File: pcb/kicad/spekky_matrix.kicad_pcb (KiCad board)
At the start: 2 copper layers, 153 x 95.8 mm, 330 parts, among them J1 USB_B_Micro, J2 Conn_ARM_JTAG_SWD_10, Q1 DMP3125L-7, Q2 DMP3125L-7, Q3 DMP3125L-7, Q4 DMP3125L-7, Q5 DMP3125L-7, Q6 DMP3125L-7, Q7 DMP3125L-7, Q8 DMP3125L-7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

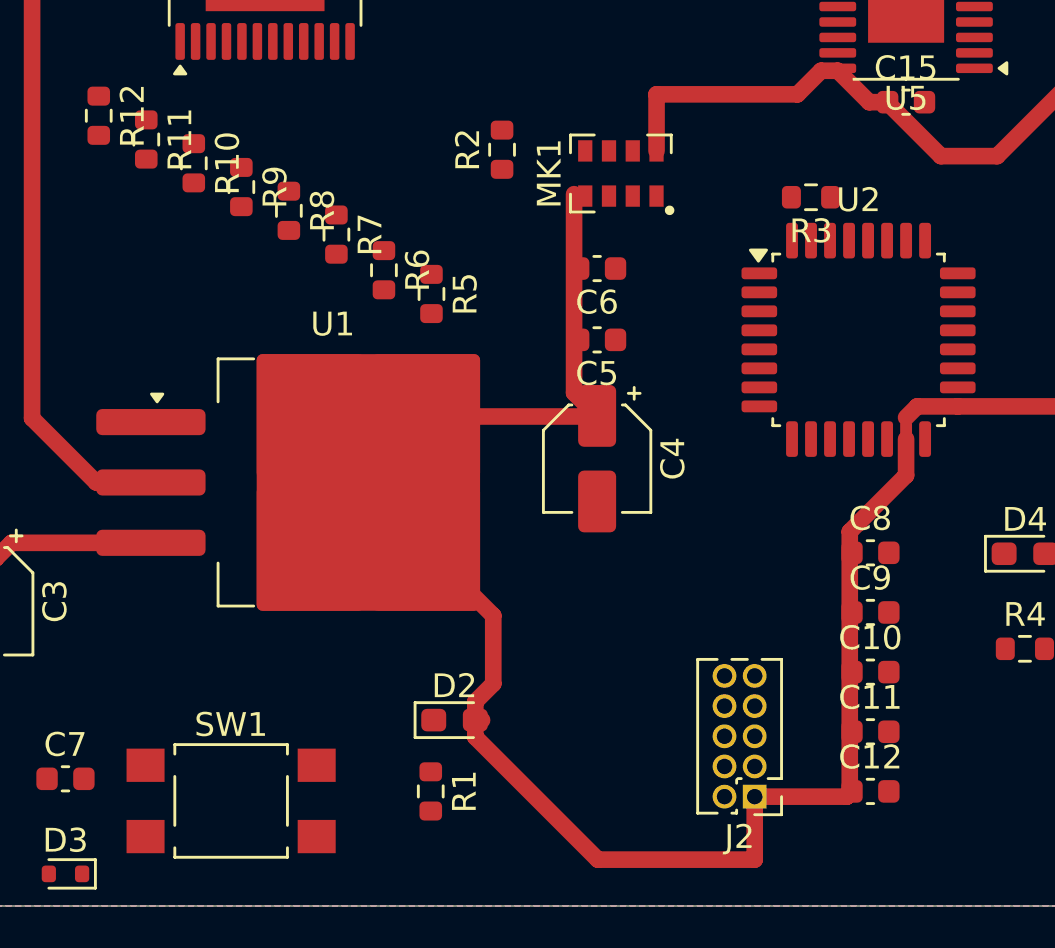
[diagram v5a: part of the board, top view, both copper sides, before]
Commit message: Rework 3v3 connections
- All 3V3 nets are now connected
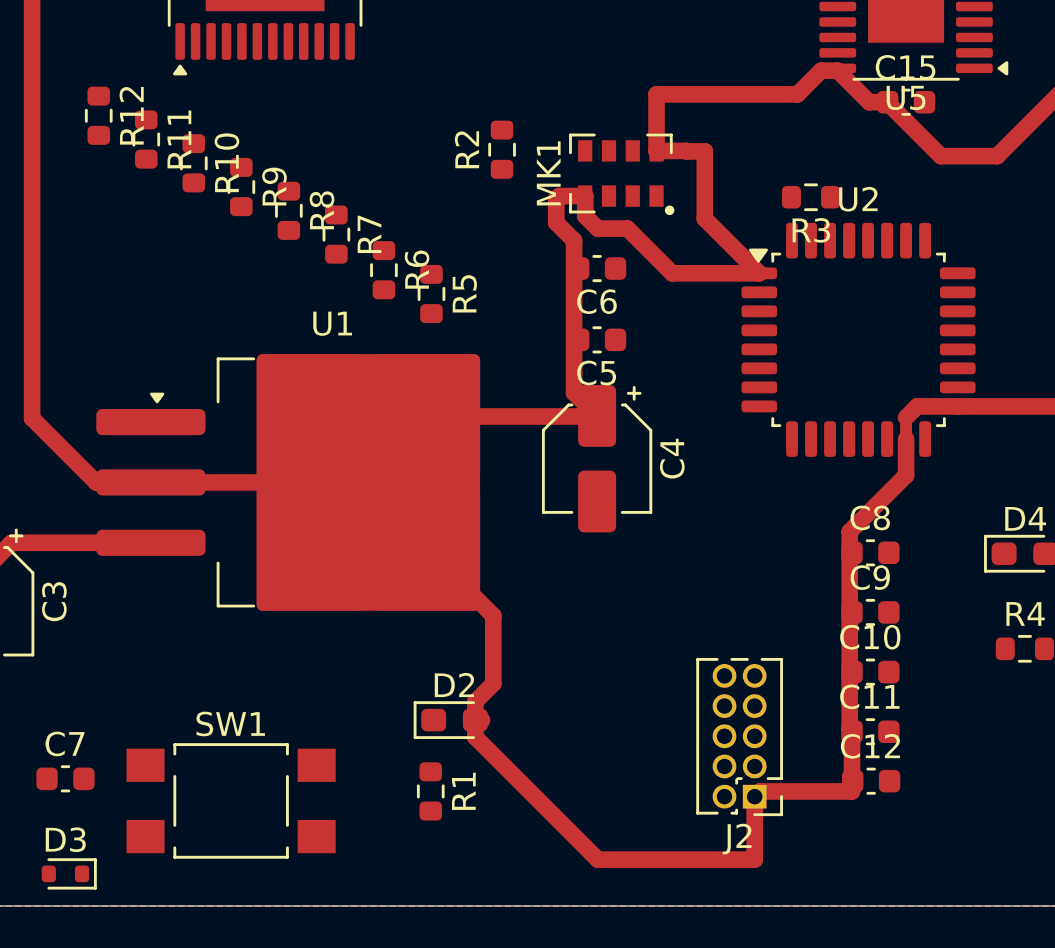
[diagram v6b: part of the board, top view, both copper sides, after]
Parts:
- moved C12 0.43 mm to (120.5, 127.5)
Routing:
- net +3V3: track 143.1 -> 170.7 mm
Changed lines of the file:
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@@
 	(footprint "Capacitor_SMD:C_0603_1608Metric"
 		(layer "F.Cu")
-		(at 120.47 127.93)
+		(at 120.5 127.5)
 		(descr "Capacitor SMD 0603 (1608 Metric), square (rectangular) end terminal, IPC_7351 nominal, (Body size source: IPC-SM-782 page 76, https://www.pcb-3d.com/wordpress/wp-content/uploads/ipc-sm-782a_amendment_1_and_2.pdf), generated with kicad-footprint-generator")
 		(tags "capacitor")
@@
 	)
 	(segment
+		(start 113.5 101)
+		(end 112.75 101)
+		(width 0.7)
+		(layer "F.Cu")
+		(net 4)
+	)
+	(segment
 		(start 115.6 130.8)
 		(end 115.6 128.15)
@@
 	)
 	(segment
+		(start 119.6 117)
+		(end 121.97 114.63)
+		(width 0.7)
+		(layer "F.Cu")
+		(net 4)
+	)
+	(segment
 		(start 103.845 124.93)
 		(end 104.13 124.93)
@@
 	)
 	(segment
-		(start 103.845 125.645)
-		(end 109 130.8)
+		(start 119.695 125.42)
+		(end 119.6 125.325)
 		(width 0.7)
 		(layer "F.Cu")
@@
 	)
 	(segment
-		(start 115.6 128.15)
-		(end 119.475 128.15)
+		(start 103.845 125.645)
+		(end 109 130.8)
 		(width 0.7)
 		(layer "F.Cu")
@@
 	)
 	(segment
-		(start 119.6 117)
-		(end 121.97 114.63)
+		(start 129.095 97.905)
+		(end 130.12 98.93)
 		(width 0.7)
 		(layer "F.Cu")
@@
 	)
 	(segment
-		(start 129.095 97.905)
-		(end 130.12 98.93)
+		(start 108.945 112.155)
+		(end 108.97 112.13)
 		(width 0.7)
 		(layer "F.Cu")
@@
 	)
 	(segment
-		(start 108.945 112.155)
-		(end 108.97 112.13)
+		(start 112.13 106.13)
+		(end 115.795 106.13)
 		(width 0.7)
 		(layer "F.Cu")
@@
 	)
 	(segment
+		(start 112.73 100.98)
+		(end 111.47 100.98)
+		(width 0.7)
+		(layer "F.Cu")
+		(net 4)
+	)
+	(segment
 		(start 121.195 98.958664)
 		(end 123.436336 101.2)
@@
 	)
 	(segment
-		(start 108 111.16)
-		(end 108 102.8)
+		(start 122.435528 111.73)
+		(end 121.969 112.196528)
 		(width 0.7)
 		(layer "F.Cu")
@@
 	)
 	(segment
-		(start 119.475 128.15)
-		(end 119.695 127.93)
+		(start 115.795 106.13)
+		(end 113.5 103.835)
 		(width 0.7)
 		(layer "F.Cu")
@@
 	)
 	(segment
-		(start 122.435528 111.73)
-		(end 121.969 112.196528)
+		(start 88.025 90.625)
+		(end 91.324 90.625)
 		(width 0.7)
 		(layer "F.Cu")
@@
 	)
 	(segment
-		(start 88.025 90.625)
-		(end 91.324 90.625)
+		(start 103.845 124.93)
+		(end 103.845 125.645)
 		(width 0.7)
 		(layer "F.Cu")
@@
 	)
 	(segment
-		(start 103.845 124.93)
-		(end 103.845 125.645)
+		(start 107.25 103)
+		(end 107.37 102.88)
 		(width 0.7)
 		(layer "F.Cu")
@@
 	)
 	(segment
-		(start 121.97 114.63)
-		(end 121.97 113.105)
+		(start 90.195 114.93)
+		(end 99.345 114.93)
+		(width 0.7)
+		(layer "F.Cu")
+		(net 4)
+	)
+	(segment
+		(start 109 104.25)
+		(end 110.25 104.25)
+		(width 0.7)
+		(layer "F.Cu")
+		(net 4)
+	)
+	(segment
+		(start 119.6 125.325)
+		(end 119.6 117)
 		(width 0.7)
 		(layer "F.Cu")
@@
 	)
 	(segment
-		(start 119.475 128.15)
-		(end 119.6 128.025)
+		(start 108.47 103.72)
+		(end 109 104.25)
 		(width 0.7)
 		(layer "F.Cu")
@@
 	)
 	(segment
+		(start 108 104.75)
+		(end 107.25 104)
+		(width 0.7)
+		(layer "F.Cu")
+		(net 4)
+	)
+	(segment
 		(start 85.195 93.93)
 		(end 85.195 93.455)
@@
 	)
 	(segment
+		(start 110.25 104.25)
+		(end 112.13 106.13)
+		(width 0.7)
+		(layer "F.Cu")
+		(net 4)
+	)
+	(segment
+		(start 107.25 104)
+		(end 107.25 103)
+		(width 0.7)
+		(layer "F.Cu")
+		(net 4)
+	)
+	(segment
 		(start 129.66 111.73)
 		(end 131.195 110.195)
@@
 	)
 	(segment
-		(start 119.6 128.025)
-		(end 119.6 117)
+		(start 115.6 128.15)
+		(end 115.819 127.931)
+		(width 0.7)
+		(layer "F.Cu")
+		(net 4)
+	)
+	(segment
+		(start 108 111.16)
+		(end 108 104.75)
+		(width 0.7)
+		(layer "F.Cu")
+		(net 4)
+	)
+	(segment
+		(start 113.5 103.835)
+		(end 113.5 101)
+		(width 0.7)
+		(layer "F.Cu")
+		(net 4)
+	)
+	(segment
+		(start 112.75 101)
+		(end 112.73 100.98)
+		(width 0.7)
+		(layer "F.Cu")
+		(net 4)
+	)
+	(segment
+		(start 115.819 127.931)
+		(end 119.695 127.931)
+		(width 0.7)
+		(layer "F.Cu")
+		(net 4)
+	)
+	(segment
+		(start 108.47 102.88)
+		(end 108.47 103.72)
 		(width 0.7)
 		(layer "F.Cu")
@@
 	)
 	(segment
+		(start 121.97 114.63)
+		(end 121.97 113.105)
+		(width 0.7)
+		(layer "F.Cu")
+		(net 4)
+	)
+	(segment
+		(start 107.37 102.88)
+		(end 108.47 102.88)
+		(width 0.7)
+		(layer "F.Cu")
+		(net 4)
+	)
+	(segment
 		(start 85.195 93.455)
 		(end 88.025 90.625)
@@
 		(width 0.7)
 		(layer "F.Cu")
+		(net 4)
+	)
+	(segment
+		(start 119.695 127.931)
+		(end 119.695 125.42)
+		(width 0.7)
+		(layer "F.Cu")

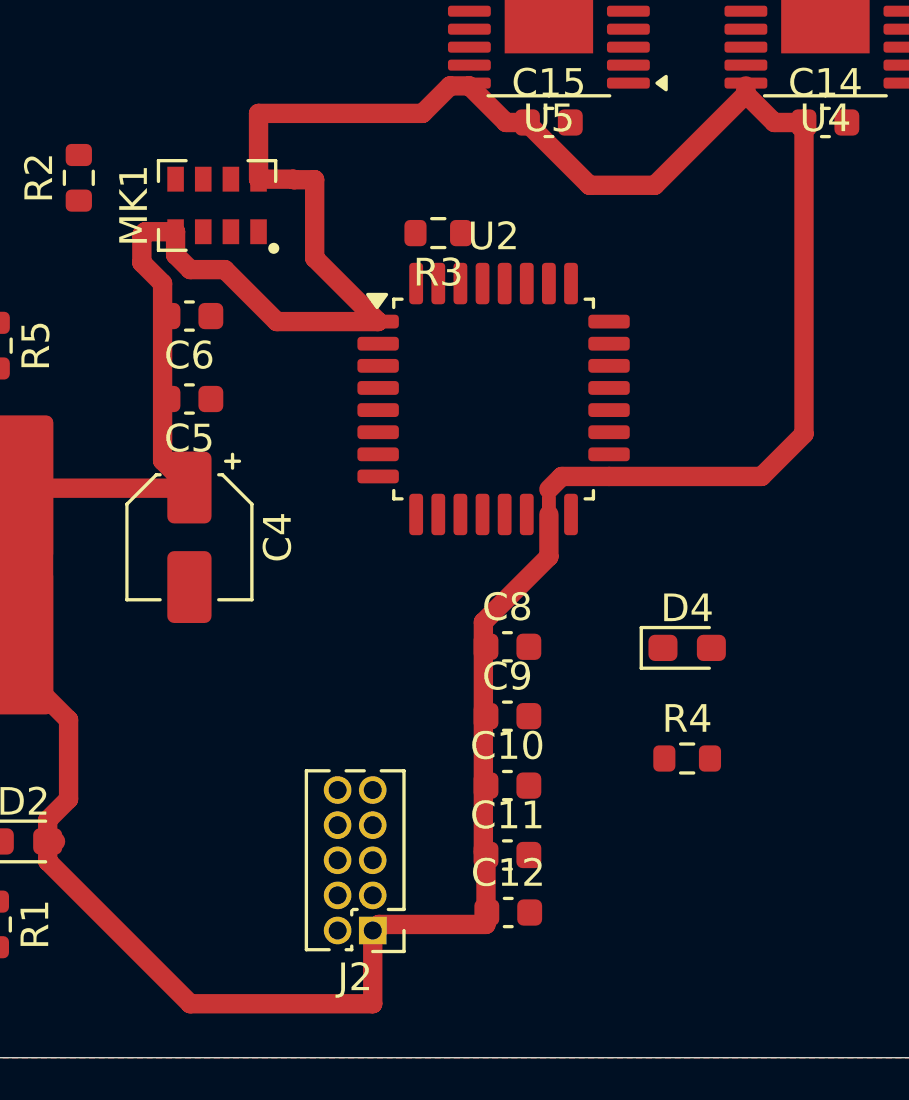
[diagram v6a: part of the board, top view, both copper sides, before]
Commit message: Move stm32 capacitors closer to stm32
- Capacitors are much more closer to the stm32 where appropriate
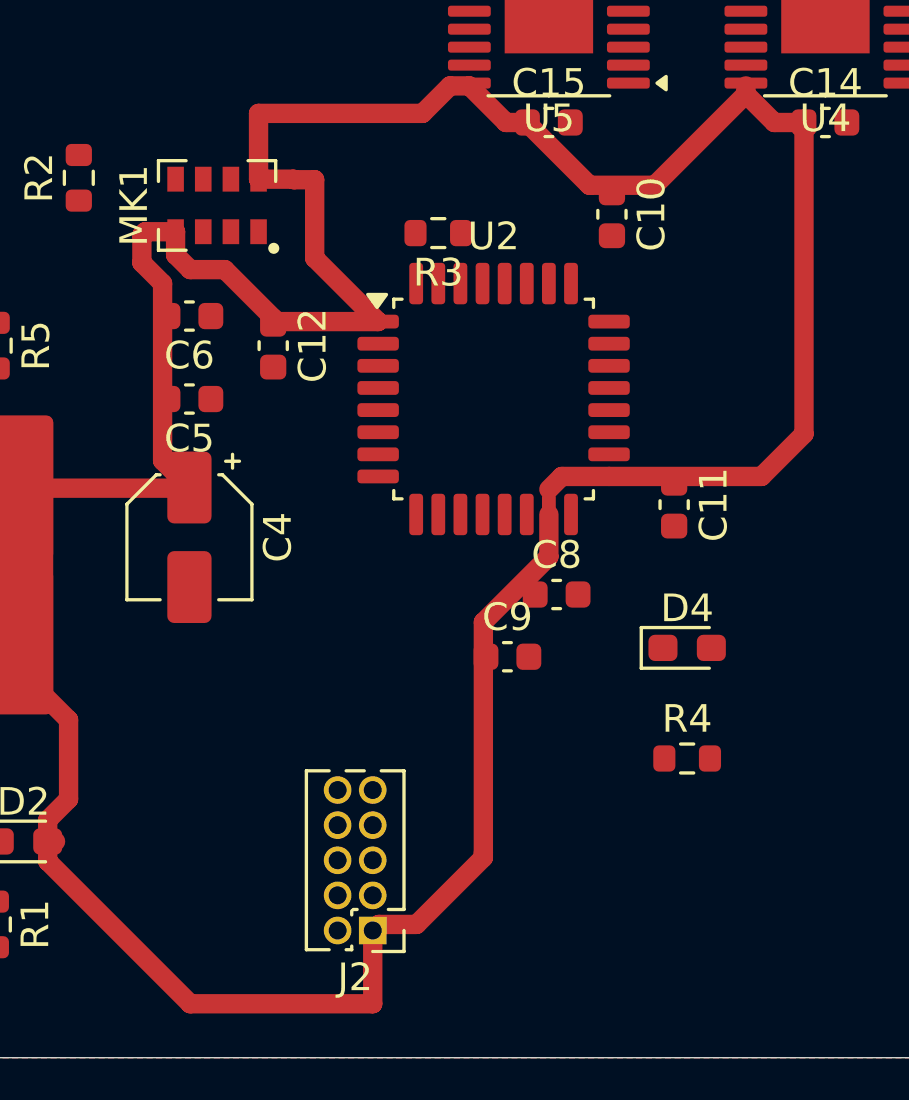
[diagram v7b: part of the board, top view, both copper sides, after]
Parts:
- moved C12 22.2 mm to (112.0, 107.0), turned to -90 degrees
- moved C10 21.0 mm to (124.2, 102.2), turned to -90 degrees
- moved C11 14.0 mm to (126.5, 112.8), turned to -90 degrees
- moved C8 2.60 mm to (122.2, 116.0)
- moved C9 2.15 mm to (120.5, 118.2)
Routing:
- net +3V3: track 170.7 -> 169.3 mm

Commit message: Update gndref net to gnd
- Changes applied to schematic and PCB
- Using GNDREF symbol for GND but need to change the net name
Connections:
- C13 pad 2: GNDREF -> GND
- C14 pad 2: GNDREF -> GND
- C15 pad 2: GNDREF -> GND
- H1 pad 1: GNDREF -> GND
- H2 pad 1: GNDREF -> GND
- H3 pad 1: GNDREF -> GND
- H4 pad 1: GNDREF -> GND
- JP1 pad 1: GNDREF -> GND
- R21 pad 1: GNDREF -> GND
- R22 pad 1: GNDREF -> GND
- R23 pad 1: GNDREF -> GND
- R24 pad 1: GNDREF -> GND
- R25 pad 1: GNDREF -> GND
- R26 pad 1: GNDREF -> GND
- R27 pad 1: GNDREF -> GND
- R28 pad 1: GNDREF -> GND
- RV1 pad 1: GNDREF -> GND
- U3 pad 1: GNDREF -> GND
- U3 pad 25: GNDREF -> GND
- U4 pad 1: GNDREF -> GND
- U4 pad 25: GNDREF -> GND
- U5 pad 1: GNDREF -> GND
- U5 pad 25: GNDREF -> GND
